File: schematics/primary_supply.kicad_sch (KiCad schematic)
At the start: 0 parts

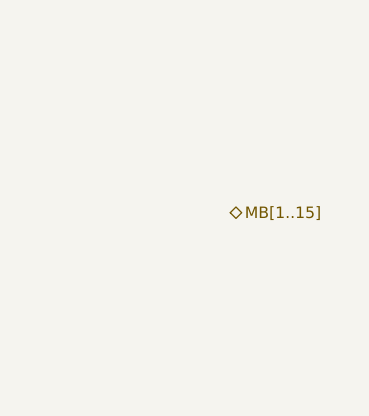
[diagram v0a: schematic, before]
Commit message: Moved more components into hierachical sheets, misc cleanup
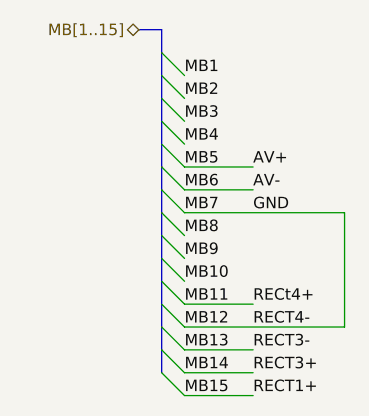
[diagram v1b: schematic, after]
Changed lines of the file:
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@@
 (kicad_sch (version 20211123) (generator eeschema)
   (paper "A4")
-  (hierarchical_label "MB[1..15]" (shape bidirectional) (at 63.5 91.44 0)
-    (effects (font (size 1.27 1.27)) (justify left))
+  (bus_entry (at 55.88 73.66) (size 2.54 2.54)
+    (stroke (width 0) (type default) (color 0 0 0 0))
+  )
+  (bus_entry (at 55.88 76.2) (size 2.54 2.54)
+    (stroke (width 0) (type default) (color 0 0 0 0))
+  )
+  (bus_entry (at 55.88 78.74) (size 2.54 2.54)
+    (stroke (width 0) (type default) (color 0 0 0 0))
+  )
+  (bus_entry (at 55.88 88.9) (size 2.54 2.54)
+    (stroke (width 0) (type default) (color 0 0 0 0))
+  )
+  (bus_entry (at 55.88 91.44) (size 2.54 2.54)
+    (stroke (width 0) (type default) (color 0 0 0 0))
+  )
+  (bus_entry (at 55.88 93.98) (size 2.54 2.54)
+    (stroke (width 0) (type default) (color 0 0 0 0))
+  )
+  (bus_entry (at 55.88 96.52) (size 2.54 2.54)
+    (stroke (width 0) (type default) (color 0 0 0 0))
+  )
+  (bus_entry (at 55.88 99.06) (size 2.54 2.54)
+    (stroke (width 0) (type default) (color 0 0 0 0))
+  )
+  (bus_entry (at 55.88 101.6) (size 2.54 2.54)
+    (stroke (width 0) (type default) (color 0 0 0 0))
+  )
+  (bus_entry (at 55.88 104.14) (size 2.54 2.54)
+    (stroke (width 0) (type default) (color 0 0 0 0))
+  )
+  (bus_entry (at 55.88 106.68) (size 2.54 2.54)
+    (stroke (width 0) (type default) (color 0 0 0 0))
+  )
+  (bus_entry (at 55.88 109.22) (size 2.54 2.54)
+    (stroke (width 0) (type default) (color 0 0 0 0))
+  )
+  (bus_entry (at 55.88 81.28) (size 2.54 2.54)
+    (stroke (width 0) (type default) (color 0 0 0 0))
+  )
+  (bus_entry (at 55.88 83.82) (size 2.54 2.54)
+    (stroke (width 0) (type default) (color 0 0 0 0))
+  )
+  (bus_entry (at 55.88 86.36) (size 2.54 2.54)
+    (stroke (width 0) (type default) (color 0 0 0 0))
+  )
+  (bus (pts (xy 55.88 81.28) (xy 55.88 83.82))
+    (stroke (width 0) (type default) (color 0 0 0 0))
+  )
+  (wire (pts (xy 58.42 101.6) (xy 66.04 101.6))
+    (stroke (width 0) (type default) (color 0 0 0 0))
+  )
+  (bus (pts (xy 55.88 99.06) (xy 55.88 101.6))
+    (stroke (width 0) (type default) (color 0 0 0 0))
+  )
+  (bus (pts (xy 55.88 83.82) (xy 55.88 86.36))
+    (stroke (width 0) (type default) (color 0 0 0 0))
+  )
+  (bus (pts (xy 55.88 86.36) (xy 55.88 88.9))
+    (stroke (width 0) (type default) (color 0 0 0 0))
+  )
+  (wire (pts (xy 58.42 104.14) (xy 76.2 104.14))
+    (stroke (width 0) (type default) (color 0 0 0 0))
+  )
+  (wire (pts (xy 58.42 86.36) (xy 66.04 86.36))
+    (stroke (width 0) (type default) (color 0 0 0 0))
+  )
+  (wire (pts (xy 58.42 106.68) (xy 66.04 106.68))
+    (stroke (width 0) (type default) (color 0 0 0 0))
+  )
+  (bus (pts (xy 53.34 71.12) (xy 55.88 71.12))
+    (stroke (width 0) (type default) (color 0 0 0 0))
+  )
+  (bus (pts (xy 55.88 76.2) (xy 55.88 78.74))
+    (stroke (width 0) (type default) (color 0 0 0 0))
+  )
+  (bus (pts (xy 55.88 73.66) (xy 55.88 76.2))
+    (stroke (width 0) (type default) (color 0 0 0 0))
+  )
+  (wire (pts (xy 76.2 104.14) (xy 76.2 91.44))
+    (stroke (width 0) (type default) (color 0 0 0 0))
+  )
+  (bus (pts (xy 55.88 101.6) (xy 55.88 104.14))
+    (stroke (width 0) (type default) (color 0 0 0 0))
+  )
+  (bus (pts (xy 55.88 78.74) (xy 55.88 81.28))
+    (stroke (width 0) (type default) (color 0 0 0 0))
+  )
+  (bus (pts (xy 55.88 71.12) (xy 55.88 73.66))
+    (stroke (width 0) (type default) (color 0 0 0 0))
+  )
+  (bus (pts (xy 55.88 91.44) (xy 55.88 93.98))
+    (stroke (width 0) (type default) (color 0 0 0 0))
+  )
+  (wire (pts (xy 58.42 88.9) (xy 66.04 88.9))
+    (stroke (width 0) (type default) (color 0 0 0 0))
+  )
+  (bus (pts (xy 55.88 104.14) (xy 55.88 106.68))
+    (stroke (width 0) (type default) (color 0 0 0 0))
+  )
+  (wire (pts (xy 58.42 91.44) (xy 76.2 91.44))
+    (stroke (width 0) (type default) (color 0 0 0 0))
+  )
+  (wire (pts (xy 58.42 109.22) (xy 66.04 109.22))
+    (stroke (width 0) (type default) (color 0 0 0 0))
+  )
+  (bus (pts (xy 55.88 93.98) (xy 55.88 96.52))
+    (stroke (width 0) (type default) (color 0 0 0 0))
+  )
+  (bus (pts (xy 55.88 88.9) (xy 55.88 91.44))
+    (stroke (width 0) (type default) (color 0 0 0 0))
+  )
+  (bus (pts (xy 55.88 96.52) (xy 55.88 99.06))
+    (stroke (width 0) (type default) (color 0 0 0 0))
+  )
+  (wire (pts (xy 58.42 111.76) (xy 66.04 111.76))
+    (stroke (width 0) (type default) (color 0 0 0 0))
+  )
+  (bus (pts (xy 55.88 106.68) (xy 55.88 109.22))
+    (stroke (width 0) (type default) (color 0 0 0 0))
+  )
+  (label "GND" (at 66.04 91.44 0)
+    (effects (font (size 1.27 1.27)) (justify left bottom))
+  )
+  (label "RECT3+" (at 66.04 109.22 0)
+    (effects (font (size 1.27 1.27)) (justify left bottom))
+  )
+  (label "MB1" (at 58.42 76.2 0)
+    (effects (font (size 1.27 1.27)) (justify left bottom))
+  )
+  (label "RECT3-" (at 66.04 106.68 0)
+    (effects (font (size 1.27 1.27)) (justify left bottom))
+  )
+  (label "RECt4+" (at 66.04 101.6 0)
+    (effects (font (size 1.27 1.27)) (justify left bottom))
+  )
+  (label "MB2" (at 58.42 78.74 0)
+    (effects (font (size 1.27 1.27)) (justify left bottom))
+  )
+  (label "MB4" (at 58.42 83.82 0)
+    (effects (font (size 1.27 1.27)) (justify left bottom))
+  )
+  (label "AV-" (at 66.04 88.9 0)
+    (effects (font (size 1.27 1.27)) (justify left bottom))
+  )
+  (label "MB14" (at 58.42 109.22 0)
+    (effects (font (size 1.27 1.27)) (justify left bottom))
+  )
+  (label "MB12" (at 58.42 104.14 0)
+    (effects (font (size 1.27 1.27)) (justify left bottom))
+  )
+  (label "MB11" (at 58.42 101.6 0)
+    (effects (font (size 1.27 1.27)) (justify left bottom))
+  )
+  (label "MB9" (at 58.42 96.52 0)
+    (effects (font (size 1.27 1.27)) (justify left bottom))
+  )
+  (label "AV+" (at 66.04 86.36 0)
+    (effects (font (size 1.27 1.27)) (justify left bottom))
+  )
+  (label "MB10" (at 58.42 99.06 0)
+    (effects (font (size 1.27 1.27)) (justify left bottom))
+  )
+  (label "MB7" (at 58.42 91.44 0)
+    (effects (font (size 1.27 1.27)) (justify left bottom))
+  )
+  (label "MB5" (at 58.42 86.36 0)
+    (effects (font (size 1.27 1.27)) (justify left bottom))
+  )
+  (label "MB3" (at 58.42 81.28 0)
+    (effects (font (size 1.27 1.27)) (justify left bottom))
+  )
+  (label "RECT4-" (at 66.04 104.14 0)
+    (effects (font (size 1.27 1.27)) (justify left bottom))
+  )
+  (label "RECT1+" (at 66.04 111.76 0)
+    (effects (font (size 1.27 1.27)) (justify left bottom))
+  )
+  (label "MB15" (at 58.42 111.76 0)
+    (effects (font (size 1.27 1.27)) (justify left bottom))
+  )
+  (label "MB13" (at 58.42 106.68 0)
+    (effects (font (size 1.27 1.27)) (justify left bottom))
+  )
+  (label "MB6" (at 58.42 88.9 0)
+    (effects (font (size 1.27 1.27)) (justify left bottom))
+  )
+  (label "MB8" (at 58.42 93.98 0)
+    (effects (font (size 1.27 1.27)) (justify left bottom))
+  )
+  (hierarchical_label "MB[1..15]" (shape bidirectional) (at 53.34 71.12 180)
+    (effects (font (size 1.27 1.27)) (justify right))
   )
 )

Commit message: cleanup, fixes, started on power supplies
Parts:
- added C? (x4): 330u, symbol Device:C_Polarized_Small
- added C? (x4): 100n, symbol Device:C_Small
- added FS5, FS? (x3): Fuse_Small, symbol Device:Fuse_Small
- added RECT1, RECT2, RECT3, RECT4: D_Bridge_-AA+, symbol Device:D_Bridge_-AA+
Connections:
- new net: C?.2, RECT1.1 (-)
- new net: C?.1, RECT1.2
- new net: FS?.2, RECT1.3
- new net: C?.1, RECT1.4 (+)
- new net: C?.1, RECT2.4 (+)
- new net: C?.2, RECT2.1 (-)
- new net: C?.1, RECT3.4 (+)
- new net: C?.2, RECT3.1 (-)
- new net: C?.2, FS?.1 (x3)
- new net: C?.2, FS5.1
- new net: FS5.2, RECT2.3
- new net: C?.1, RECT4.2
- new net: C?.1, RECT2.2
- new net: C?.1, RECT3.2
- new net: C?.2, RECT4.1 (-)
- new net: FS?.2, RECT4.3
- new net: C?.1, RECT4.4 (+)
- new net: FS?.2, RECT3.3

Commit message: More power supply work
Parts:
- removed C? (x4): 330u, symbol Device:C_Polarized_Small
- removed C? (x4): 100n, symbol Device:C_Small
- removed FS5, FS? (x3): Fuse_Small, symbol Device:Fuse_Small
- added C11, C37, C38, C55: 10n, symbol Device:C_Small
- added C17, C18, C19, C20, C42: 100n, symbol Device:C_Small
- added C22, C24: 1m, symbol Device:C_Polarized_Small
- added C24: 2m2, symbol Device:C_Polarized_Small
- added C25: 3m3, symbol Device:C_Polarized_Small
- added C25: 330u, symbol Device:C_Polarized_Small
- added C33, C34: 22u, symbol Device:C_Polarized_Small
- added C39, C40: 100u, symbol Device:C_Polarized_Small
- added C41: 470p, symbol Device:C_Small
- added D13, D8: 1N4004, Diode_THT:D_DO-201AD_P15.24mm_Horizontal, symbol Custom:1N4004
- added D14, D15, D16, D5, D6, D? (x2): 1N914, Diode_THT:D_DO-201AD_P15.24mm_Horizontal, symbol Custom:1N914
- added D25, D26, D27, D28, D30, D31, D32, D33: 1N5404, Diode_THT:D_DO-201AD_P15.24mm_Horizontal, symbol Custom:1N5404
- added D7: BYV95A, Diode_THT:D_DO-201AD_P15.24mm_Horizontal, symbol Custom:BYV95A
- added D? (x2): 1N4148, Diode_THT:D_DO-35_SOD27_P7.62mm_Horizontal, symbol Diode:1N4148
- added FS1: Fuse_Small, symbol Device:Fuse_Small
- added HS1, HS2, HS3, HS4, HS5: Heatsink, symbol Mechanical:Heatsink
- added L1: L, symbol Custom:L
- added PLA: Conn_01x12_Male, symbol Connector:Conn_01x12_Male
- added PLB: Conn_01x08_Male, symbol Connector:Conn_01x08_Male
- added R11, R16: 3k3, symbol Device:R_Small
- added R14, R32, R53, R57: 10k, symbol Device:R_Small
- added R15, R52, R9: 2k2, symbol Device:R_Small
- added R17: 2.7k, symbol Device:R_Small
- added R18, R23: 100, symbol Device:R_Small
- added R19, R20, R56, R? (x2): 1k, symbol Device:R_Small
- added R27, R28: 58, symbol Device:R_Small
- added R35: 470k, symbol Device:R_Small
- added R37, R51: 100k, symbol Device:R_Small
- added R38, R47: 14k, symbol Device:R_Small
- added R42: 0.15, symbol Device:R_Small
- added R43: 0.68, symbol Device:R_Small
- added R58: 560R, symbol Device:R_Small
- added R8: 470, symbol Device:R_Small
- added REG1: L7815, symbol Regulator_Linear:L7815
- added REG2: L7915, symbol Regulator_Linear:L7915
- added SK1: Conn_01x15_Female, symbol Connector:Conn_01x15_Female
- added TR1: MPSA42, Package_TO_SOT_THT:TO-92_Inline, symbol Transistor_BJT:MPSA42
- added TR2, TR3: MPDA42, Package_TO_SOT_THT:TO-92_Inline, symbol Transistor_BJT:MPSA42
- added TR4: 2N3904, Package_TO_SOT_THT:TO-92_Inline, symbol Transistor_BJT:2N3904
- added TR5: 2N3906, Package_TO_SOT_THT:TO-92_Inline, symbol Transistor_BJT:2N3906
- added TR6: IRF9631, symbol Custom:IRF9631
- added TR7: IRF540, symbol Custom:IRF540
- added TR8: IRF9531, symbol Custom:IRF9531
- added U?: LF347, symbol Custom:LF347
- added U?: OP27, symbol Custom:OP27
- added U?: OP07, symbol Amplifier_Operational:OP07
- added U?: LF411, symbol Custom:LF411
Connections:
- net AV+: now also C33.1, REG1.3 (OUT), SK1.5 (Pin_5), U?.4 (V+), U?.7 (V+), U?.7 (V+)
- net AV-: now also C34.2, REG2.3 (VO), SK1.6 (Pin_6), U?.11 (V-), U?.4 (V-), U?.4 (V-)
- net RECT1-: now reaches RECT1.1 (-)
- net RECT1-: now also C24.2, REG2.2 (VI)
- net AC_IN10: now reaches RECT1.2
- net AC_IN10: now also C17.1, PLA.10 (Pin_10)
- net AC_IN12: now reaches RECT1.3
- net AC_IN12: now also C17.2, PLA.12 (Pin_12)
- net PS15: now reaches RECT1.4 (+)
- net PS15: now also C22.1, REG1.1 (IN), SK1.15 (Pin_15)
- net RECT2+: now reaches RECT2.4 (+)
- net RECT2+: now also C25.1, R14.1, TR6.3
- net RECT2-: now reaches RECT2.1 (-)
- net RECT2-: now also C25.2, D7., TR1.1 (E)
- net PS14: now reaches RECT3.4 (+)
- net PS14: now also C24.1, SK1.14 (Pin_14)
- net PS13: now reaches RECT3.1 (-)
- net PS13: now also C24.2, SK1.13 (Pin_13)
- net at RECT2.3: now also FS1.2
- net AC_IN9: now reaches RECT4.2
- net AC_IN9: now also C20.1, PLA.9 (Pin_9)
- net AC_IN4: now reaches RECT2.2
- net AC_IN4: now also C18.1, PLA.4 (Pin_4)
- net AC_IN5: now reaches RECT3.2
- net AC_IN5: now also C19.1, PLA.5 (Pin_5)
- net AC_IN11: now reaches RECT4.1 (-)
- net AC_IN11: now also C22.2, C24.1, C25.2, C33.2, C34.1, D14., PLA.11 (Pin_11), R53.1, REG1.2 (GND), REG2.1 (GND), SK1.12 (Pin_12), SK1.7 (Pin_7), TR3.1 (E)
- net AC_IN8: now reaches RECT4.3
- net AC_IN8: now also C20.2, PLA.8 (Pin_8)
- net PS11: now reaches RECT4.4 (+)
- net PS11: now also C25.1, SK1.11 (Pin_11)
- net AC_IN6: now reaches RECT3.3
- net AC_IN6: now also C19.2, PLA.6 (Pin_6)
- new net: C41.1, D15., D16., TR2.3 (C), U?.3 (+)
- new net: C41.2, R56.2, TR2.2 (B)
- new net: C55.1, R37.1, R38.2, U?.9 (I3-)
- new net: C55.2, L1., R37.2
- new net: D25., D28., D30., R20.2, R28.1, TR8.2
- new net: D5., D6., R27.2, R28.2, TR4.3 (C), TR5.3 (C)
- new net: C11.1, R35.1, U?.10 (I3+)
- new net: C11.2, R32.2, R35.2, TR1.2 (B)
- new net: C37.2, R11.2, R23.1, R9.1, TR4.1 (E)
- new net: R47.1, R51.2, U?.12 (I4+)
- new net: R32.1, U?.8 (O3)
- new net: R18.2, TR8.1
- new net: D32., R19.2, R27.1, TR8.3
- new net: D31., TR7.3
- new net: C37.1, C38.1, R11.1, R16.1, R8.2
- new net: D26., D27.
- new net: D25., D26.
- new net: D7., L1., TR6.2
- new net: D14., TR2.1 (E)
- new net: R23.2, TR7.1
- new net: R52.2, R56.1
- new net: R14.2, R17.1, TR6.1
- new net: D30., D33., R42.1, R43.1
- new net: C42.1, U?.6
- new net: C42.2, R58.2
- new net: D15., R57.1, U?.2 (-)
- new net: C38.2, R15.1, R16.2, R18.1, TR5.1 (E)
- new net: D?., D?.
- new net: D?., D?., R?.1
- new net: R17.2, TR1.3 (C)
- new net: R38.1, R47.2
- new net: D32., R43.2
- new net: D?.1 (K), D?.2 (A), R?.1, R?.2
- new net: D27., D28.
- new net: R52.1, R53.2, TR3.2 (B)
- new net: R20.1, TR4.2 (B)
- new net: D33., TR7.2
- new net: R19.1, TR5.2 (B)
- new net: D16., R58.1
- new net AC_IN1: C39.2, C40.1, D31., D5., D6., D?.1 (K), D?.2 (A), PLA.1 (Pin_1), R42.2, R51.1, R?.2
- new net AC_IN2: D13., D8., PLA.2 (Pin_2)
- new net AC_IN3: C18.2, FS1.1, PLA.3 (Pin_3)
- new net AC_IN7: PLA.7 (Pin_7)
- new net AV+_ISO: C39.1, D13., R9.2, U?.7 (V+)
- new net AV-_ISO: C40.2, D8., R15.2, U?.4 (V-)
- new net CC_MODE: SK1.2 (Pin_2)
- new net D_OUT1: PLB.1 (Pin_1)
- new net D_OUT2: PLB.2 (Pin_2)
- new net D_OUT3: PLB.3 (Pin_3)
- new net D_OUT4: PLB.4 (Pin_4)
- new net D_OUT5: PLB.5 (Pin_5)
- new net D_OUT6: PLB.6 (Pin_6)
- new net D_OUT7: PLB.7 (Pin_7)
- new net D_OUT8: PLB.8 (Pin_8)
- new net IREF: SK1.4 (Pin_4)
- new net I_OUT_V+: SK1.1 (Pin_1)
- new net I_OUT_V-: SK1.9 (Pin_9)
- new net OEN: SK1.8 (Pin_8)
- new net PS10: R57.2, SK1.10 (Pin_10)
- new net PS3: SK1.3 (Pin_3)
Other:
- note added: "-17V switching VGS pulse on TR1"
- note added: "AC_IN1,2 = 25.6VAC AC_IN3 = NC AC_IN4,5 = 91.6VAC AC_IN6,7 = 25VAC AC_IN8,9 = 16VAC AC_IN10,12 = 92.6VAC AC_IN11 = GND"
- note added: "D_OUT1 = REAR IO V+ SENSE D_OUT2 = NC D_OUT3 = FRONT IO V+ OUT D_OUT4 = REAR IO V+ OUT D_OUT5 = REAR_IO_VCOM_OUT D_OUT6 = FRONT_IO_VCOM_OUT D_OUT7 = REAR_IO_VCOM_SENSE D_OUT8 = NC"
- note added: "PS3 is probable cv target/voltage limit reference voltage PS4 is probably cc target/current limit reference voltage"
- note added: "TR3 is rsponsible for driving the relay"
- note added: "Voltage across D27 and D28 in series varies with voltage and current"

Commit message: Update to KiCad v8.0
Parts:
- renumbered C24 to C26, C25 to C32, TR5 to TR4, TR4 to TR5
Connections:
- net at D26.: now also D25.; no longer D27.
- net at D?., D?.: now also R?.1
- new net: D26., D27.
- new net: D?., D?.

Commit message: Updated to KiCad v10.0. Minor improvements.
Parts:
- added HS6: Heatsink, symbol Mechanical:Heatsink
- added L2: L, symbol Custom:L
- added TR9: IRF9631, symbol Custom:IRF9631
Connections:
- net AC_IN5: no longer C19.1, RECT3.2
- net AC_IN6: now also C19.1, RECT3.2; no longer C19.2, RECT3.3
- net AC_IN7: now also C19.2, RECT3.3
- net at D26.: now also D25.; no longer D27.
- net at D?., D?.: now also R?.1
- net at D33., TR7.2: now also L2.
- new net: D26., D27.
- new net: D?., D?.
- new net: L2., TR9.2
